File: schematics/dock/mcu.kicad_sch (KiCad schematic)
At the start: 10 parts, among them J1 programmer, U4 STM32L476RGTx

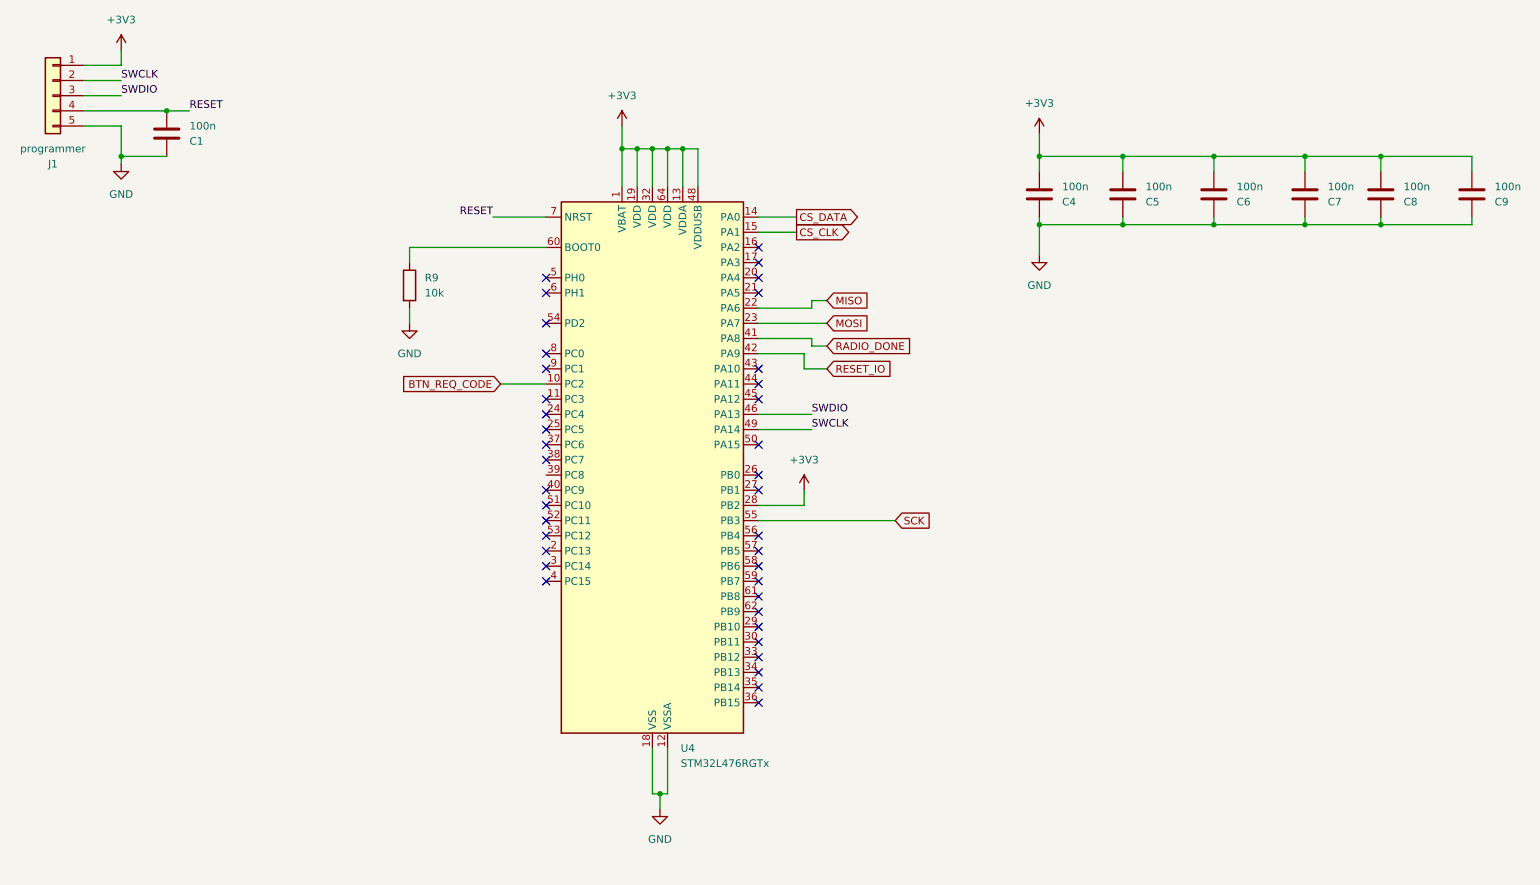
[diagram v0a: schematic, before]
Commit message: Added various tests, started work on off-board controller
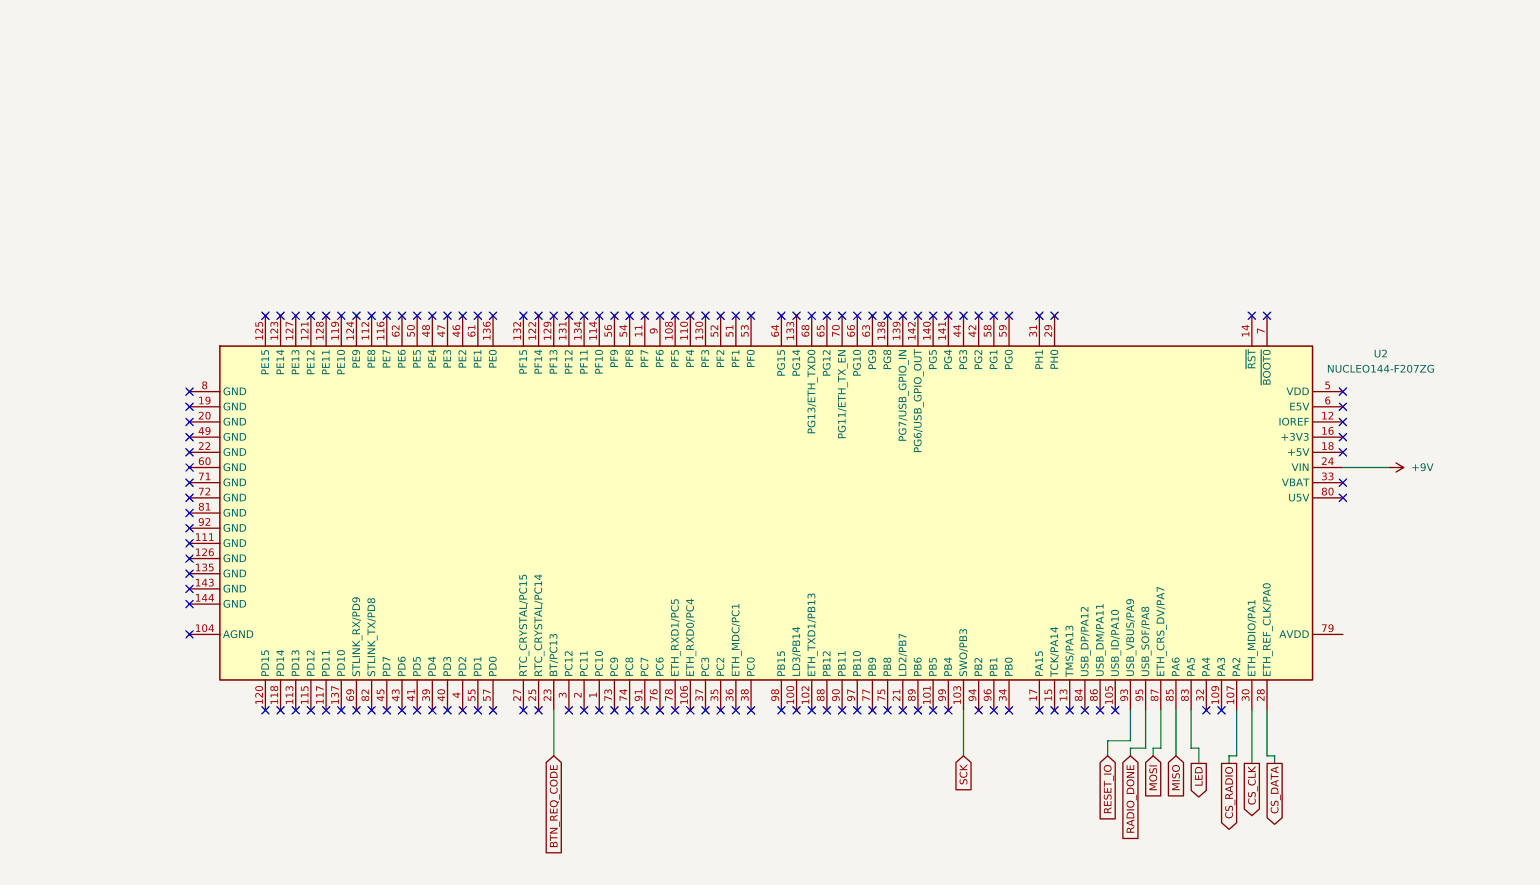
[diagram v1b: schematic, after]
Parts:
- removed C1, C4, C5, C6, C7, C8, C9: 100n, Capacitor_SMD:C_0805_2012Metric_Pad1.18x1.45mm_HandSolder, symbol Device:C
- removed J1: programmer, Connector_PinSocket_2.54mm:PinSocket_1x05_P2.54mm_Vertical, symbol Connector_Generic:Conn_01x05
- removed R9: 10k, Resistor_SMD:R_0805_2012Metric_Pad1.20x1.40mm_HandSolder, symbol Device:R
- removed U4: STM32L476RGTx, Package_QFP:LQFP-64_10x10mm_P0.5mm, symbol MCU_ST_STM32L4:STM32L476RGTx
- added U2: NUCLEO144-F207ZG, Module:ST_Morpho_Connector_144_STLink, symbol MCU_Module:NUCLEO144-F207ZG
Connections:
- net BTN_REQ_CODE: now also U2.23 (BT/PC13)
- net CS_CLK: now also U2.30 (ETH_MDIO/PA1)
- net CS_DATA: now also U2.28 (ETH_REF_CLK/PA0)
- net MISO: now also U2.85 (PA6)
- net MOSI: now also U2.87 (ETH_CRS_DV/PA7)
- net RADIO_DONE: now also U2.95 (USB_SOF/PA8)
- net RESET_IO: now also U2.93 (USB_VBUS/PA9)
- net SCK: now also U2.103 (SWO/PB3)
- new net +9V: U2.24 (VIN)
- new net CS_RADIO: U2.107 (PA2)
- new net LED: U2.83 (PA5)
- no-connect marks 39 -> 129

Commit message: Added dock code
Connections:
- net CS_CLK renamed DISPLAY_CLK
- net CS_DATA renamed DISPLAY_DATA
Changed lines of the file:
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@@
 		)
 	)
-	(global_label "CS_DATA"
+	(global_label "DISPLAY_DATA"
 		(shape output)
 		(at 229.87 144.78 270)
@@
 		)
 	)
-	(global_label "CS_CLK"
+	(global_label "DISPLAY_CLK"
 		(shape output)
 		(at 226.06 144.78 270)
